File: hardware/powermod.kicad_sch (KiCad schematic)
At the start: 69 parts, among them J1 USB_C_IN, J2 USB_C_OUT, J3 JST_PH_2, J4 STEMMA_QT, J5 UPDI_HDR, Q1 AON7407, Q2 AON7407, Q3 BSS138, SW1 BUTTON, U1 BM8563, U2 ATtiny1617, U3 TPS63020DSJR, U4 TP4056, U5 XC6206P332MR, Y1 32.768kHz

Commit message: KiCad verification: ERC clean, round-trip connectivity proven
kicad-cli 10.0.4 now installed. Iterated the generator: lib_symbols
need the full library prefix; placement grid moved to 1.27mm multiples;
generated powermod.kicad_sym + sym-lib-table + fp-lib-table so all
references resolve. Every footprint verified to exist on disk —
TPS63020's VSON-14 traced to a TI drawing, LEDs moved to 4-pad PLCC4
(the C155 candidate was reverse-mount), switch to PTS647, exact Sumida
inductor name.

Final state: ERC = 0 violations, and 'kicad-cli sch export netlist'
produces connectivity IDENTICAL to our generated powermod.net (44 nets,
same membership) — KiCad's own engine derives from the schematic
exactly the netlist the spec intends.

Co-Authored-By: Claude Opus 4.8 <noreply@anthropic.com>
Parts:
- D1, D2: value LED_RG_CC -> LED_RG_PLCC4; footprint LED_SMD:LED_LTST-C155GEKT -> LED_SMD:LED_Avago_PLCC4_3.2x2.8mm_CW
- L1: footprint Inductor_SMD:L_Sumida_CDMC6D28 -> Inductor_SMD:L_Sumida_CDMC6D28_7.25x6.5mm
- Q1, Q2: footprint Package_DFN_QFN:DFN-8-1EP_3x3mm_P0.65mm -> Package_DFN_QFN:DFN-8-1EP_3x3mm_P0.65mm_EP1.6x2.56mm
- SW1: footprint Button_Switch_SMD:SW_SPST_PTS645 -> Button_Switch_SMD:SW_SPST_PTS647_Sx50
- U3: footprint Package_SON:VSON-14-1EP_3.5x3.5mm_P0.5mm -> Package_SON:VSON-14-1EP_3x4.45mm_P0.65mm_EP1.6x4.2mm_ThermalVias
- U4: footprint Package_SO:SOIC-8-1EP_3.9x4.9mm_P1.27mm_EP2.29x2.29mm -> Package_SO:SOIC-8-1EP_3.9x4.9mm_P1.27mm_EP2.29x3mm
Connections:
- net 3V3: now also C14.1, C9.1, D3.2 (A), J5.2 (3V3), R15.1, R16.1, R17.1, R18.1, R19.1, R27.1, U2.4 (VDD), U5.2 (VOUT)
- net BUTTON: now also SW1.1 (A), U2.19 (PC2/BUTTON)
- net CC1_IN: now also J1.A5 (CC1), R2.1
- net CC1_OUT: now also J2.A5 (CC1), R4.1
- net CC2_IN: now also J1.B5 (CC2), R3.1
- net CC2_OUT: now also J2.B5 (CC2), R5.1
- net CHG_CE: now also U2.21 (PC4/CHG_CE), U4.8 (CE)
- net CHG_CHRG: now also R15.2, U2.12 (PB4/CHG_CHRG), U4.7 (CHRG)
- net CHG_JP: now also JP1.1 (A), R27.2
- net CHG_STDBY: now also R16.2, U2.11 (PB5/CHG_STDBY), U4.6 (STDBY)
- net CONV_EN: now also R14.1, U2.2 (PA3/CONV_EN), U3.12 (EN)
- net D1_GRN: now also D1.3 (A_GRN), R21.2
- net D1_RED: now also D1.1 (A_RED), R20.2
- net D2_GRN: now also D2.3 (A_GRN), R23.2
- net D2_RED: now also D2.1 (A_RED), R22.2
- net FB: now also R24.1, R25.1, U3.3 (FB)
- net FB_MID: now also JP2.1 (A), R25.2, R26.1
- net GND: now also C1.2, C10.2, C11.2, C13.2, C14.2, C15.2, C16.2, C2.2, C3.2, C4.2, C5.2, C6.2, C7.2, C8.2, C9.2, D1.2 (K_RED), D1.4 (K_GRN), D2.2 (K_RED), D2.4 (K_GRN), J1.A1 (GND), J1.A12 (GND), J1.B1 (GND), J1.B12 (GND), J1.S1 (SHIELD), J2.A1 (GND), J2.A12 (GND), J2.B1 (GND), J2.B12 (GND), J2.S1 (SHIELD), J3.2 (BAT-), J4.1 (GND), J5.3 (GND), Q3.2 (S), R1.2, R12.2, R13.2, R14.2, R2.2, R24.2, R3.2, R7.2, R9.2, SW1.2 (B), TP4.1 (P), U1.4 (VSS), U2.3 (GND), U2.EP (PAD), U3.13 (PS/SYNC), U3.2 (GND), U3.EP (PGND), U4.1 (TEMP), U4.3 (GND), U4.EP (PAD), U5.1 (VSS)
- net L1N: now also L1.1, U3.8 (L1), U3.9 (L1)
- net L2: now also L1.2, U3.6 (L2), U3.7 (L2)
- net LED_BAT_A: now also R22.1, U2.10 (PB6/LED_BAT_A)
- net LED_BAT_B: now also R23.1, U2.9 (PB7/LED_BAT_B)
- net LED_PWR_A: now also R20.1, U2.14 (PB2/LED_PWR_A)
- net LED_PWR_B: now also R21.1, U2.13 (PB3/LED_PWR_B)
- net OSCI: now also U1.1 (OSCI), Y1.1 (X1)
- net OSCO: now also U1.2 (OSCO), Y1.2 (X2)
- net PROG: now also R1.1, U4.2 (PROG)
- net Q1_GATE: now also C12.2, Q1.4 (G), R10.2, R11.1
- net Q1_GATE_DRV: now also Q3.1 (G), R13.1, U2.20 (PC3/Q1_GATE_DRV)
- net Q3_DRAIN: now also Q3.3 (D), R11.2
- net RTC_INT: now also R19.2, U1.3 (INT), U2.1 (PA2/RTC_INT)
- net RTC_SCL: now also R18.2, U1.6 (SCL), U2.18 (PC1/RTC_SCL)
- net RTC_SDA: now also R17.2, U1.5 (SDA), U2.17 (PC0/RTC_SDA)
- net RTC_VDD: now also C13.1, D3.1 (K), D4.1 (K), U1.8 (VDD)
- net SCL: now also J4.4 (SCL), U2.16 (PB0/SCL)
- net SDA: now also J4.3 (SDA), U2.15 (PB1/SDA)
- net UPDI: now also J5.1 (UPDI), U2.23 (PA0/UPDI)
- net VBACKUP: now also D4.2 (A), JP1.2 (B), TP1.1 (P)
- net VBAT: now also C6.1, J3.1 (BAT+), Q2.5 (D), Q2.6 (D), Q2.7 (D), Q2.8 (D), Q2.EP (D), R6.1, TP2.1 (P), U4.5 (BAT)
- net VBAT_DIV: now also C10.1, R6.2, R7.1, U2.5 (PA4/VBAT_SENSE)
- net VBUS: now also C15.1, C7.1, J1.A4 (VBUS), J1.A9 (VBUS), J1.B4 (VBUS), J1.B9 (VBUS), Q1.5 (D), Q1.6 (D), Q1.7 (D), Q1.8 (D), Q1.EP (D), Q2.4 (G), R12.1, R8.1, U4.4 (VCC)
- net VBUS_DIV: now also C11.1, R8.2, R9.1, U2.6 (PA5/VBUS_SENSE)
- net VOUT: now also C3.1, C4.1, C5.1, J2.A4 (VBUS), J2.A9 (VBUS), J2.B4 (VBUS), J2.B9 (VBUS), JP2.2 (B), R26.2, R4.2, R5.2, TP3.1 (P), U3.4 (VOUT), U3.5 (VOUT)
- net VSYS: now also C1.1, C12.1, C16.1, C2.1, C8.1, Q1.1 (S), Q1.2 (S), Q1.3 (S), Q2.1 (S), Q2.2 (S), Q2.3 (S), R10.1, U3.1 (VINA), U3.10 (VIN), U3.11 (VIN), U5.3 (VIN)

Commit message: Layout: placed, DRC-clean board (routing pending)
hardware/layout.py: floorplan-as-code. Parses real footprint geometry
from the installed KiCad libraries, places all 69 components + 4 M2
holes on a 62x46mm 2-layer outline, binds every pad to its net, pours
GND both sides. Floorplan encodes the checklist: power flows J1 ->
charger/OR -> converter -> J2 left to right; crystal ~36mm from the
inductor loop; connectors on edges.

Iterated under kicad-cli pcb drc: 200 violations -> 0 electrical/
mechanical. Remaining: the 160-edge ratsnest (routing deliberately not
generated) and cosmetic silk warnings. TPS63020 footprint moved to the
plain EP variant; thermal vias added manually at layout with 0.3mm
drills. Visual check: board_top.svg rendered and reviewed.

Also: .gitignore for KiCad lock/history files (project is now open in
the GUI on this machine).

Co-Authored-By: Claude Opus 4.8 <noreply@anthropic.com>
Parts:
- U3: footprint Package_SON:VSON-14-1EP_3x4.45mm_P0.65mm_EP1.6x4.2mm_ThermalVias -> Package_SON:VSON-14-1EP_3x4.45mm_P0.65mm_EP1.6x4.2mm
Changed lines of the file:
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@@
   (property "Reference" "U3" (at 670.5600000000001 148.56 0) (effects (font (size 1.27 1.27))))
   (property "Value" "TPS63020DSJR" (at 670.5600000000001 176.56 0) (effects (font (size 1.27 1.27))))
-  (property "Footprint" "Package_SON:VSON-14-1EP_3x4.45mm_P0.65mm_EP1.6x4.2mm_ThermalVias" (at 670.5600000000001 162.56 0) (effects (font (size 1.27 1.27)) hide))
+  (property "Footprint" "Package_SON:VSON-14-1EP_3x4.45mm_P0.65mm_EP1.6x4.2mm" (at 670.5600000000001 162.56 0) (effects (font (size 1.27 1.27)) hide))
   (pin "1")
   (pin "2")

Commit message: Compact re-layout: 56x40mm (-21%), paired solder pads, EP fix at source
User review caught pad-pairing defect: one shared GND pad served three
solder interfaces, 36mm from VBACKUP - 'two solder pads (VBACKUP, GND)'
was physically false. Added TP5/TP6; all three interfaces now have
adjacent ground partners.

Also: netlist.py EP keys fixed at source ('EP' -> '25'/'15'/'9' per
real footprint pad names), so regenerated boards bind exposed pads
natively. Board shrunk 62x46 -> 56x40 via scaled floorplan + edge
overrides, iterated under courtyard DRC. Freerouting re-routed the
compact board in 8-17s per cycle (115/117 edges - placement iteration
is now cheap, which IS the layout-optimization answer).

DRC: 0 shorts / 0 clearance / 0 crossings; 14 unconnected + 12 starved
thermals remain (3 unstitchable GND spokes in dense regions, 2 U2
escapes: SCL, LED_BAT_A). Hand-finish in pcbnew; not fab-ready.

Co-Authored-By: Claude Opus 4.8 <noreply@anthropic.com>
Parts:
- added TP5: VBACKUP_GND_PAD, TestPoint:TestPoint_Pad_2.0x2.0mm, symbol powermod:PM_TP5
- added TP6: VOUT_GND_PAD, TestPoint:TestPoint_Pad_2.0x2.0mm, symbol powermod:PM_TP6
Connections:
- net GND: now also U2.25 (PAD), U3.15 (PGND), U4.9 (PAD), TP5.1 (P), TP6.1 (P); no longer U2.EP (PAD), U3.EP (PGND), U4.EP (PAD)
- net VBAT: now also Q2.9 (D); no longer Q2.EP (D)
- net VBUS: now also Q1.9 (D); no longer Q1.EP (D)

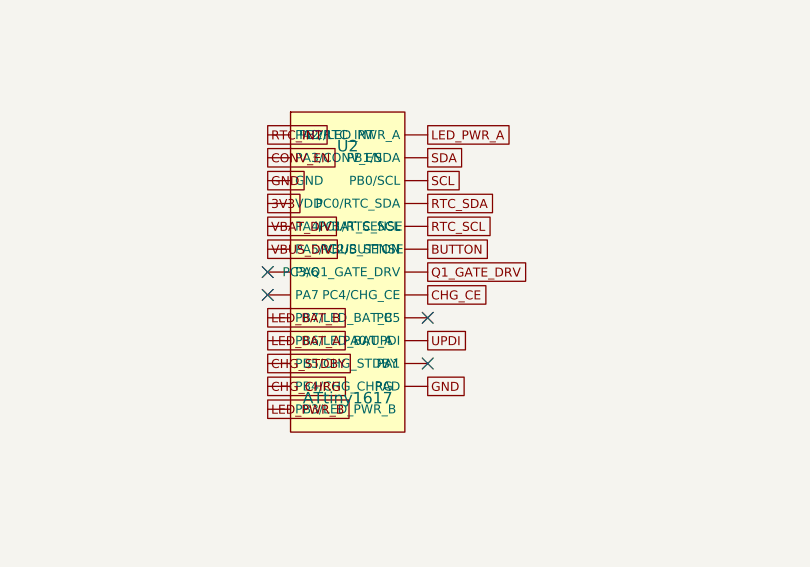
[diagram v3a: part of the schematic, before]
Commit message: checkpoint: RTC bus reassigned PC0/PC1 -> PA1/PC5 (top-side pins face the RTC)
Co-Authored-By: Claude Opus 4.8 <noreply@anthropic.com>
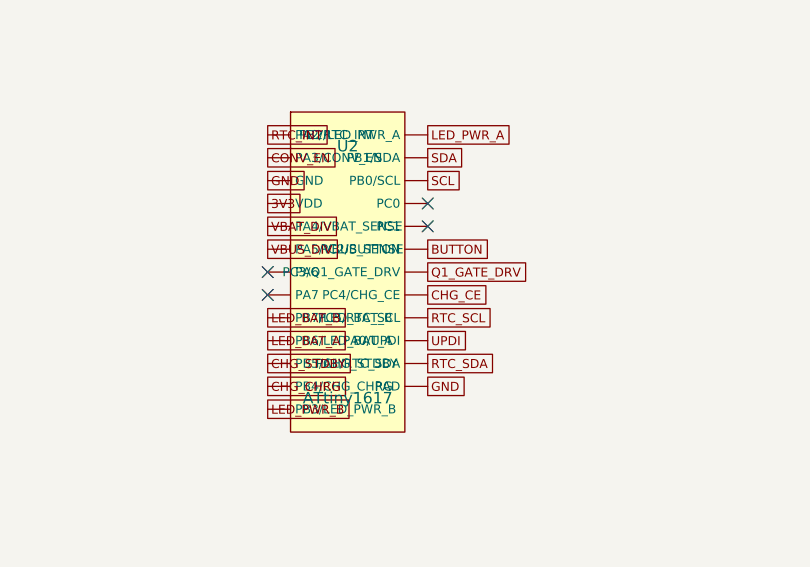
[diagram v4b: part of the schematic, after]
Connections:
- net RTC_SCL: now also U2.22 (PC5/RTC_SCL); no longer U2.18 (PC1/RTC_SCL)
- net RTC_SDA: now also U2.24 (PA1/RTC_SDA); no longer U2.17 (PC0/RTC_SDA)
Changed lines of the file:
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@@
  (global_label "SDA" (shape passive) (at 679.45 215.9 0) (effects (font (size 1.0 1.0)) (justify left)))
  (global_label "SCL" (shape passive) (at 679.45 218.44 0) (effects (font (size 1.0 1.0)) (justify left)))
- (global_label "RTC_SDA" (shape passive) (at 679.45 220.98 0) (effects (font (size 1.0 1.0)) (justify left)))
- (global_label "RTC_SCL" (shape passive) (at 679.45 223.51999999999998 0) (effects (font (size 1.0 1.0)) (justify left)))
  (global_label "BUTTON" (shape passive) (at 679.45 226.06 0) (effects (font (size 1.0 1.0)) (justify left)))
  (global_label "Q1_GATE_DRV" (shape passive) (at 679.45 228.6 0) (effects (font (size 1.0 1.0)) (justify left)))
  (global_label "CHG_CE" (shape passive) (at 679.45 231.14 0) (effects (font (size 1.0 1.0)) (justify left)))
+ (global_label "RTC_SCL" (shape passive) (at 679.45 233.68 0) (effects (font (size 1.0 1.0)) (justify left)))
  (global_label "UPDI" (shape passive) (at 679.45 236.22 0) (effects (font (size 1.0 1.0)) (justify left)))
+ (global_label "RTC_SDA" (shape passive) (at 679.45 238.76 0) (effects (font (size 1.0 1.0)) (justify left)))
  (global_label "GND" (shape passive) (at 679.45 241.29999999999998 0) (effects (font (size 1.0 1.0)) (justify left)))
  (global_label "VSYS" (shape passive) (at 661.6700000000001 285.75000000000006 0) (effects (font (size 1.0 1.0)) (justify left)))
@@
  (no_connect (at 661.6700000000001 228.6))
  (no_connect (at 661.6700000000001 231.14))
- (no_connect (at 679.45 233.68))
- (no_connect (at 679.45 238.76))
+ (no_connect (at 679.45 220.98))
+ (no_connect (at 679.45 223.51999999999998))
  (no_connect (at 679.45 298.45000000000005))
 )

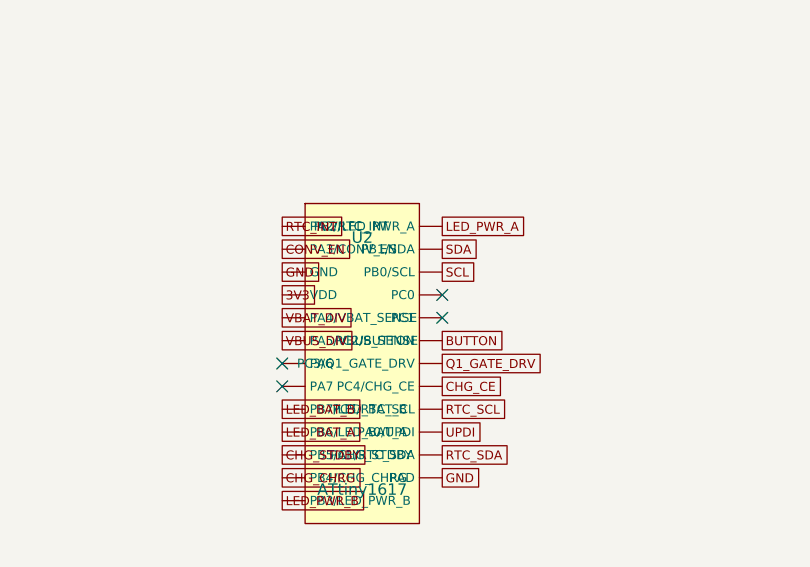
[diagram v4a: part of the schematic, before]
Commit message: checkpoint: pin swaps routed, SCL last unrouted
Co-Authored-By: Claude Opus 4.8 <noreply@anthropic.com>
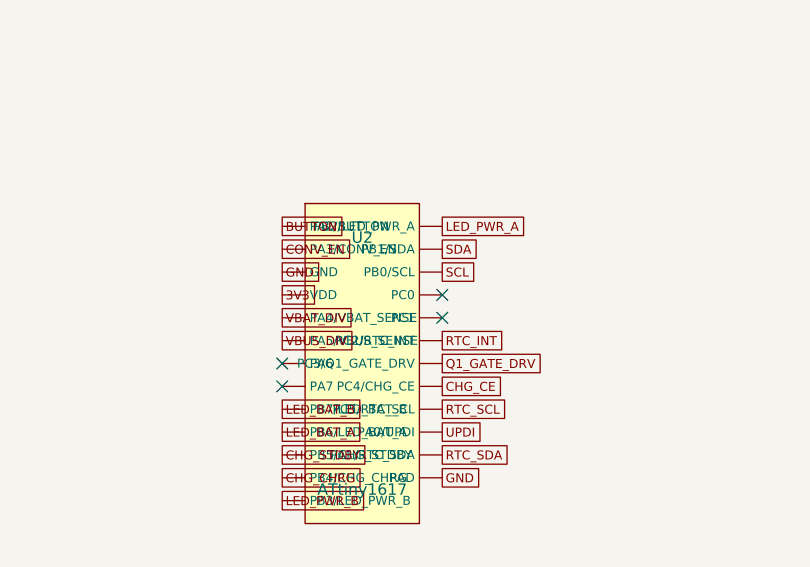
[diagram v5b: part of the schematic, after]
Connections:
- net BUTTON: now also U2.1 (PA2/BUTTON); no longer U2.19 (PC2/BUTTON)
- net RTC_INT: now also U2.19 (PC2/RTC_INT); no longer U2.1 (PA2/RTC_INT)
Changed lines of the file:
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@@
  (global_label "RTC_SCL" (shape passive) (at 679.45 161.29 0) (effects (font (size 1.0 1.0)) (justify left)))
  (global_label "RTC_VDD" (shape passive) (at 679.45 166.37 0) (effects (font (size 1.0 1.0)) (justify left)))
- (global_label "RTC_INT" (shape passive) (at 661.6700000000001 213.35999999999999 0) (effects (font (size 1.0 1.0)) (justify left)))
+ (global_label "BUTTON" (shape passive) (at 661.6700000000001 213.35999999999999 0) (effects (font (size 1.0 1.0)) (justify left)))
  (global_label "CONV_EN" (shape passive) (at 661.6700000000001 215.9 0) (effects (font (size 1.0 1.0)) (justify left)))
  (global_label "GND" (shape passive) (at 661.6700000000001 218.44 0) (effects (font (size 1.0 1.0)) (justify left)))
@@
  (global_label "SDA" (shape passive) (at 679.45 215.9 0) (effects (font (size 1.0 1.0)) (justify left)))
  (global_label "SCL" (shape passive) (at 679.45 218.44 0) (effects (font (size 1.0 1.0)) (justify left)))
- (global_label "BUTTON" (shape passive) (at 679.45 226.06 0) (effects (font (size 1.0 1.0)) (justify left)))
+ (global_label "RTC_INT" (shape passive) (at 679.45 226.06 0) (effects (font (size 1.0 1.0)) (justify left)))
  (global_label "Q1_GATE_DRV" (shape passive) (at 679.45 228.6 0) (effects (font (size 1.0 1.0)) (justify left)))
  (global_label "CHG_CE" (shape passive) (at 679.45 231.14 0) (effects (font (size 1.0 1.0)) (justify left)))

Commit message: hardware: full electrical verification pass + R28 (CE pull-up) + ADC ref
Reconfirmed the schematic against fresh datasheet evidence, not recall
(user-requested gate before continuing v1/v2 layout work):

- TPS63020: pin-function table extracted from TI's PDF -- all 14 pins +
  EP=PGND match netlist.py exactly. VFB=500mV; our JP2-closed divider is
  TI's own 3.3V table row (1M/180k); open computes 5.00V. Switch limit
  4A typ confirmed; C16 satisfies the VINA bypass rule (<=0.22uF).
- AON7407: package confirmed DFN3x3-8 EP=D (footprint correct); gate
  drives checked against the +/-8V VGS limit: Q1 -3.57V driven, Q2 worst
  +/-5.25V, all safe and past the -3.0V/25mOhm requirement point.
- OR stage walked end-to-end: body-diode orientations, default states in
  MCU reset, soft-start (C12+R11), VBUS bleed, clean charge termination
  (Q2 hard-off on mains means the charger never sees load current).
- BM8563/diode-OR: D3/D4 cathodes on RTC_VDD verified in source (netlist
  golden vectors cover them); 3.3V bus vs diode-dropped RTC_VDD is legal
  (PCF8563-class inputs rated to 6.5V independent of VDD).
- ERC 0 violations, netlist self-test passes: 72 components, 236 pins.

Two findings, both closed here:

1. R28 100k CHG_CE -> VBUS (new). Without it TP4056's CE floats whenever
   PC4 is high-Z (MCU reset, UPDI, unprogrammed) -- undefined charger
   state. Pull-UP so a dead-MCU board still charges (charging-autonomy
   policy); PC4 push-pull overrides. Placed in v2 (courtyards still 0
   overlaps, pads bind VBUS/CHG_CE). The frozen v1 board predates it --
   noted in the doc; v1 was already marked not-fab-ready.

2. ADC reference constraint documented: the spec deferred "re-check
   divider ratio vs chosen reference at schematic time" and it never
   landed. With 1M/330k, VBUS@5.25V presents 1.30V -- the 1.1V internal
   ref CLIPS. Firmware must use the 1.5V internal reference (both
   channels then fit; VBAT max 1.04V). Now in powermod-schematic.md as
   a hardware-imposed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
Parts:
- added R28: 100k, Resistor_SMD:R_0402_1005Metric, symbol powermod:PM_R28
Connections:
- net CHG_CE: now also R28.2
- net VBUS: now also R28.1
